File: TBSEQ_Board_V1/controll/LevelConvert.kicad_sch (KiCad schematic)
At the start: 2 parts, among them U1 AE-LCNV4-MOSFET, U4 AE-LCNV4-MOSFET

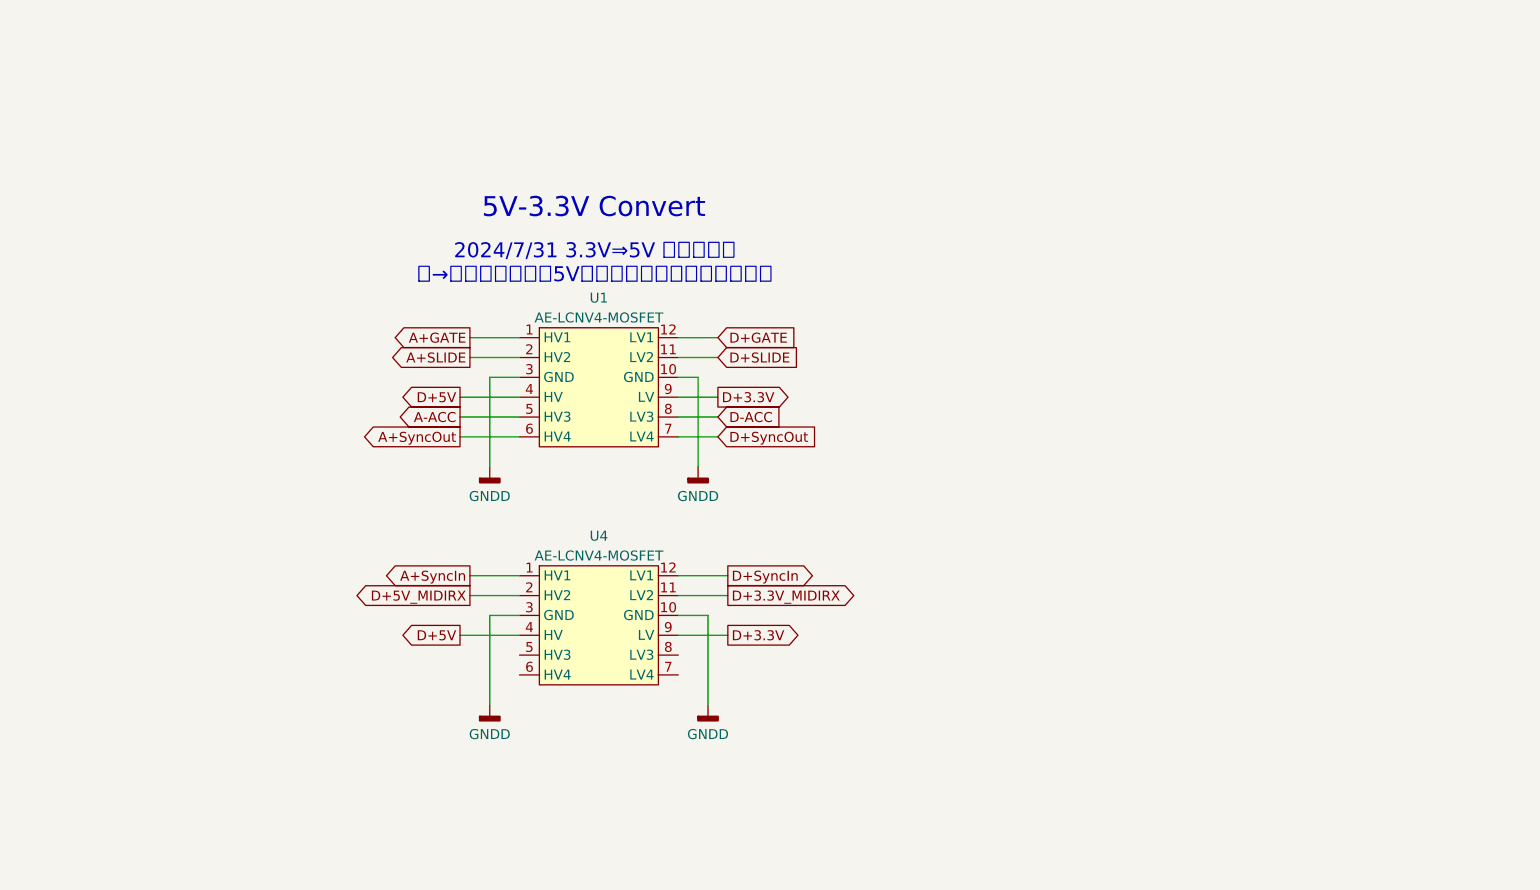
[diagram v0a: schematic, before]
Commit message: HT16K33 5VOutputBuffer
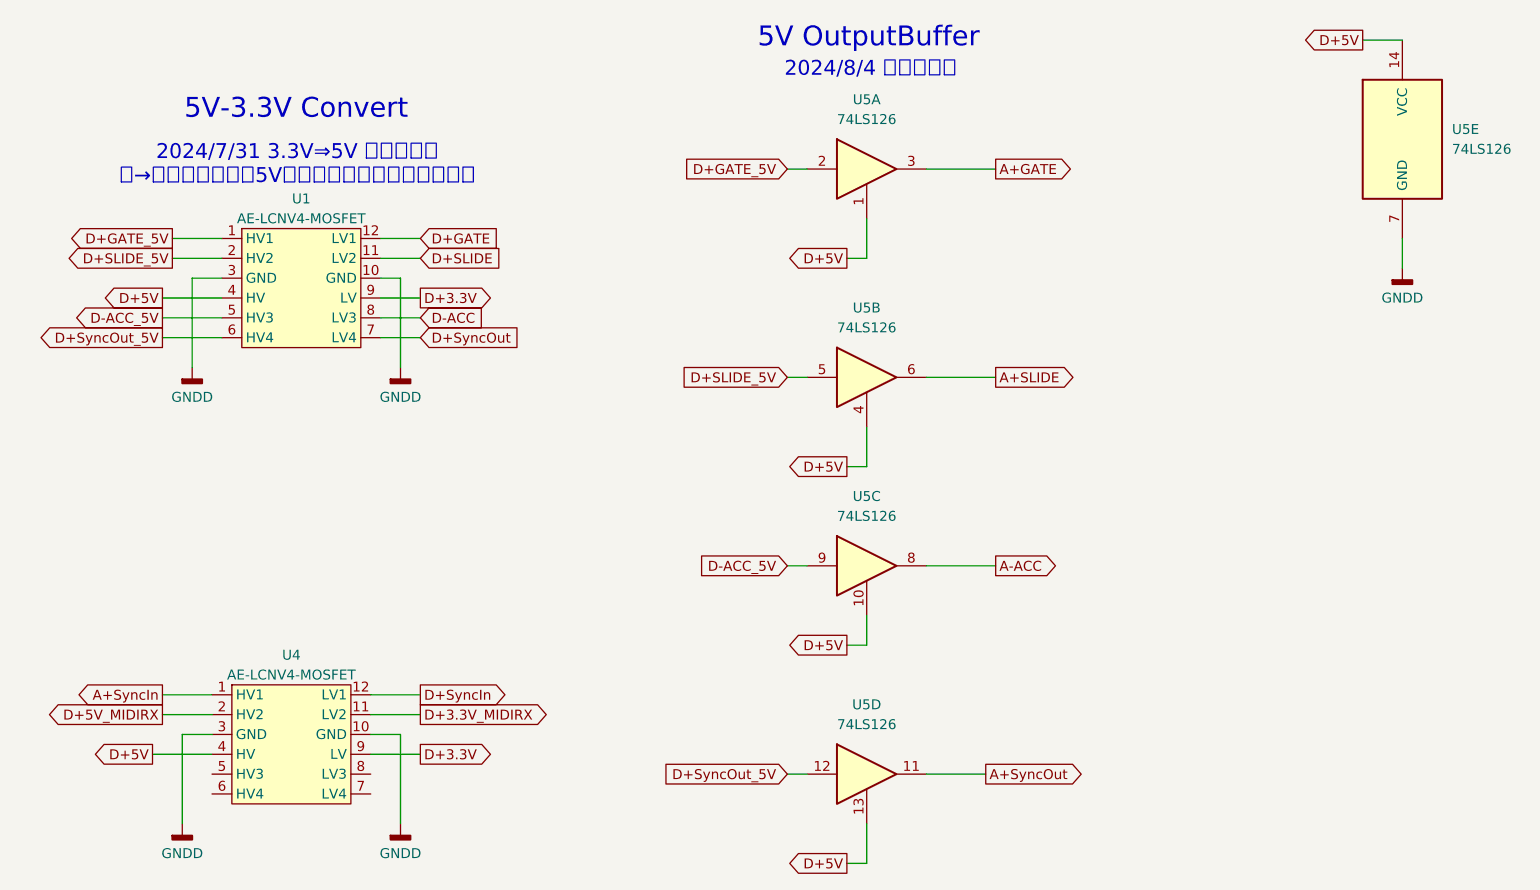
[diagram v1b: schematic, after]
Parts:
- added U5: 74LS126, symbol 74xx:74LS126
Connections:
- net A+GATE: now also U5.3; no longer U1.1 (HV1)
- net A+SLIDE: now also U5.6; no longer U1.2 (HV2)
- net A+SyncOut: now also U5.11; no longer U1.6 (HV4)
- net A-ACC: now also U5.8; no longer U1.5 (HV3)
- net D+5V: now also U5.1, U5.10, U5.13, U5.14 (VCC), U5.4
- net GNDD: now also U5.7 (GND)
- new net D+GATE_5V: U1.1 (HV1), U5.2
- new net D+SLIDE_5V: U1.2 (HV2), U5.5
- new net D+SyncOut_5V: U1.6 (HV4), U5.12
- new net D-ACC_5V: U1.5 (HV3), U5.9
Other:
- note added: "2024/8/4 動作確認済"
- note added: "5V OutputBuffer"
- moved on the sheet: U1, U4

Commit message: HT16K33Panel
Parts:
- removed U1: AE-LCNV4-MOSFET, SamacSys_Parts:CERDIP-14_W10.16mm_SideBrazed_LongPads_Socket, symbol SamacSys_Parts:AE-LCNV4-MOSFET(BSS138)
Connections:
- net D+GATE_5V is gone; now on net D+GATE: U5.2
- net D+SLIDE_5V is gone; now on net D+SLIDE: U5.5
- net D+SyncOut_5V is gone; now on net D+SyncOut: U5.12
- net D-ACC_5V is gone; now on net D-ACC: U5.9
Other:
- note added: "2024/8/5 動作確認済"
- note added: "3.3V=>5V OutputBuffer"
- note added: "5V=>3.3V Convert"
- note removed: "2024/7/31 3.3V⇒5V 動作確認済 →場合によっては5V変換後にバッファが必要かも"
- note removed: "2024/8/4 動作確認済"
- note removed: "5V OutputBuffer"
- note removed: "5V-3.3V Convert"
- moved on the sheet: U4
